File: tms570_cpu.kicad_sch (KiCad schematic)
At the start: 50 parts, among them J2 FTSH-105-01-L-DV-K, U2 TMS570LS0914PGE

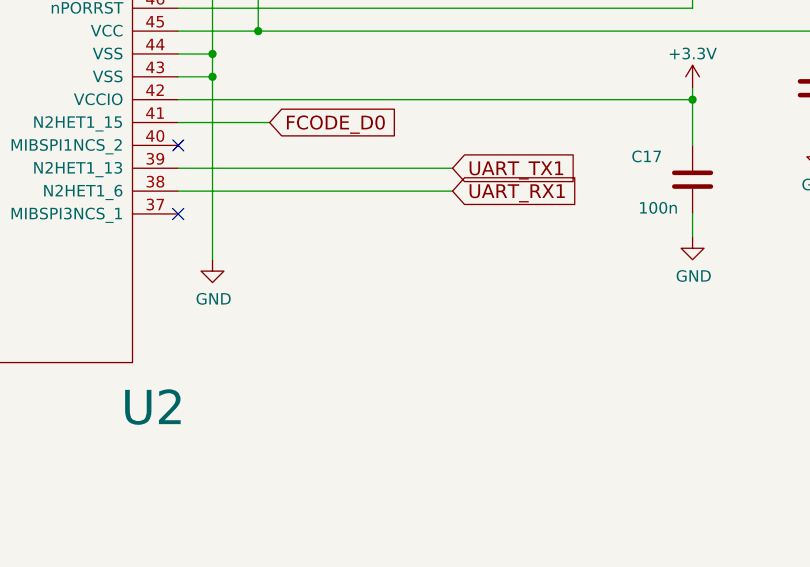
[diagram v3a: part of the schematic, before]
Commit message: Added a connector for the UART1 interface
Signed-off-by: Corey Minyard <corey@minyard.net>
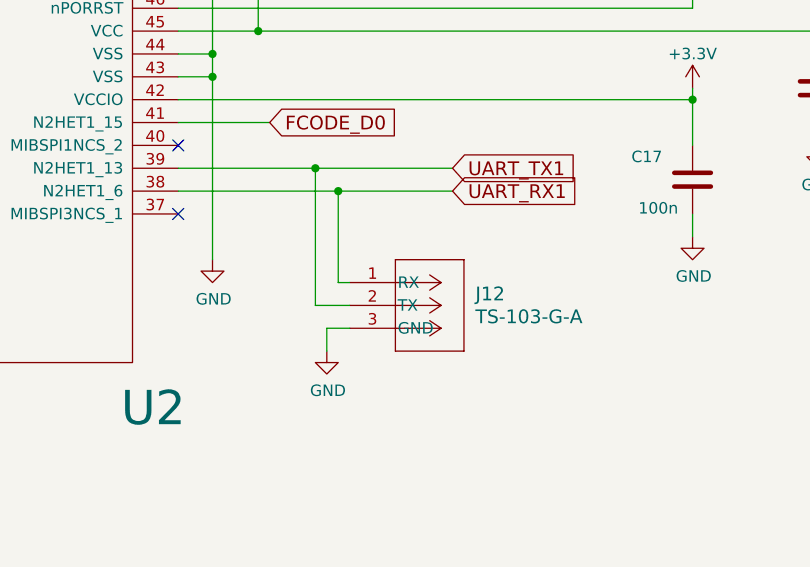
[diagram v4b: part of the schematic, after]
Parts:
- added J12: TS-103-G-A, LocalFootprints:CON3_1X3_TU_HTS_SAI, symbol PACSAT_DEV_misc:TS-103-G-A_2-UART
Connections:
- net GND: now also J12.3 (GND)
- net UART_RX1: now also J12.1 (RX)
- net UART_TX1: now also J12.2 (TX)
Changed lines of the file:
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@@
 	)
 	(junction
+		(at 297.18 177.8)
+		(diameter 0)
+		(color 0 0 0 0)
+	)
+	(junction
 		(at 237.49 207.01)
 		(diameter 0)
@@
 	)
 	(junction
+		(at 299.72 180.34)
+		(diameter 0)
+		(color 0 0 0 0)
+	)
+	(junction
 		(at 135.89 167.64)
 		(diameter 0)
@@
 	(wire
 		(pts
+			(xy 300.99 193.04) (xy 297.18 193.04)
+		)
+		(stroke
+			(width 0)
+			(type default)
+		)
+	)
+	(wire
+		(pts
 			(xy 140.97 76.2) (xy 101.6 76.2)
 		)
@@
 	(wire
 		(pts
-			(xy 281.94 180.34) (xy 312.42 180.34)
+			(xy 300.99 190.5) (xy 299.72 190.5)
+		)
+		(stroke
+			(width 0)
+			(type default)
+		)
+	)
+	(wire
+		(pts
+			(xy 281.94 180.34) (xy 299.72 180.34)
 		)
 		(stroke
@@
 	(wire
 		(pts
+			(xy 298.45 195.58) (xy 298.45 198.12)
+		)
+		(stroke
+			(width 0)
+			(type default)
+		)
+	)
+	(wire
+		(pts
 			(xy 101.6 142.24) (xy 149.86 142.24)
 		)
@@
 	(wire
 		(pts
-			(xy 281.94 177.8) (xy 312.42 177.8)
+			(xy 281.94 177.8) (xy 297.18 177.8)
 		)
 		(stroke
@@
 	(wire
 		(pts
+			(xy 299.72 180.34) (xy 312.42 180.34)
+		)
+		(stroke
+			(width 0)
+			(type default)
+		)
+	)
+	(wire
+		(pts
 			(xy 229.87 204.47) (xy 229.87 224.79)
 		)
@@
 		)
 	)
+	(wire
+		(pts
+			(xy 297.18 193.04) (xy 297.18 177.8)
+		)
+		(stroke
+			(width 0)
+			(type default)
+		)
+	)
 	(polyline
 		(pts
@@
 	(wire
 		(pts
+			(xy 297.18 177.8) (xy 312.42 177.8)
+		)
+		(stroke
+			(width 0)
+			(type default)
+		)
+	)
+	(wire
+		(pts
 			(xy 135.89 109.22) (xy 135.89 132.08)
 		)
@@
 	(wire
 		(pts
+			(xy 300.99 195.58) (xy 298.45 195.58)
+		)
+		(stroke
+			(width 0)
+			(type default)
+		)
+	)
+	(wire
+		(pts
 			(xy 121.92 139.7) (xy 149.86 139.7)
 		)
@@
 	(wire
 		(pts
+			(xy 299.72 190.5) (xy 299.72 180.34)
+		)
+		(stroke
+			(width 0)
+			(type default)
+		)
+	)
+	(wire
+		(pts
 			(xy 189.23 63.5) (xy 189.23 72.39)
 		)
@@
 	)
 	(symbol
+		(lib_id "PACSAT_DEV_misc:TS-103-G-A_2-UART")
+		(at 300.99 190.5 0)
+		(unit 1)
+		(exclude_from_sim no)
+		(in_bom yes)
+		(on_board yes)
+		(dnp no)
+		(fields_autoplaced yes)
+		(property "Reference" "J12"
+			(at 314.96 191.7699 0)
+			(effects
+				(font
+					(size 1.524 1.524)
+				)
+				(justify left)
+			)
+		)
+		(property "Value" "TS-103-G-A"
+			(at 314.96 194.3099 0)
+			(effects
+				(font
+					(size 1.524 1.524)
+				)
+				(justify left)
+			)
+		)
+		(property "Footprint" "LocalFootprints:CON3_1X3_TU_HTS_SAI"
+			(at 300.99 190.5 0)
+			(effects
+				(font
+					(size 1.27 1.27)
+					(italic yes)
+				)
+				(hide yes)
+			)
+		)
+		(property "Datasheet" "TS-103-G-A"
+			(at 300.99 190.5 0)
+			(effects
+				(font
+					(size 1.27 1.27)
+					(italic yes)
+				)
+				(hide yes)
+			)
+		)
+		(property "Description" "1x3 pin UART"
+			(at 300.99 190.5 0)
+			(effects
+				(font
+					(size 1.27 1.27)
+				)
+				(hide yes)
+			)
+		)
+		(pin "3"
+		)
+		(pin "2"
+		)
+		(pin "1"
+		)
+		(instances
+			(project ""
+				(path "/cc9f42d2-6985-41ac-acab-5ab7b01c5b38/adf61ae3-df77-4e04-8bda-b4049a36fcf4"
+					(reference "J12")
+					(unit 1)
+				)
+			)
+		)
+	)
+	(symbol
 		(lib_id "Device:R")
 		(at 228.6 24.13 0)
@@
 					(unit 1)
 				)
+			)
+		)
+	)
+	(symbol
+		(lib_id "power:GND")
+		(at 298.45 198.12 0)
+		(unit 1)
+		(exclude_from_sim no)
+		(in_bom yes)
+		(on_board yes)
+		(dnp no)
+		(property "Reference" "#PWR025"
+			(at 298.45 204.47 0)
+			(effects
+				(font
+					(size 1.27 1.27)
+				)
+				(hide yes)
+			)
+		)
+		(property "Value" "GND"
+			(at 298.577 202.5142 0)
+			(effects
+				(font
+					(size 1.27 1.27)
+				)
+			)
+		)
+		(property "Footprint" ""
+			(at 298.45 198.12 0)
+			(effects
+				(font
+					(size 1.27 1.27)
+				)
+				(hide yes)
+			)
+		)
+		(property "Datasheet" ""
+			(at 298.45 198.12 0)
+			(effects
+				(font
+					(size 1.27 1.27)
+				)
+				(hide yes)
+			)
+		)
+		(property "Description" ""
+			(at 298.45 198.12 0)
+			(effects
+				(font
+					(size 1.27 1.27)
+				)
+			)
+		)
+		(pin "1"
+		)
+		(instances
+			(project "PacSat_AFSK"
+				(path "/cc9f42d2-6985-41ac-acab-5ab7b01c5b38/adf61ae3-df77-4e04-8bda-b4049a36fcf4"
+					(reference "#PWR025")
+					(unit 1)
+				)

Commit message: Add 4 more MRAM parts
Signed-off-by: Corey Minyard <corey@minyard.net>
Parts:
- J12: footprint LocalFootprints:CON3_1X3_TU_HTS_SAI -> PacSatDev_misc:CON3_1X3_TU_HTS_SAI
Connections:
- net MRAM_NCS3: now reaches U2.37 (MIBSPI3NCS_1)
- net MRAM_NCS2: now reaches U2.40 (MIBSPI1NCS_2)
- net MRAM_NCS1: now reaches U2.54 (MIBSPI3NENA)
- net PWR_FLAG_LNA: now reaches U2.75 (AD1IN_11)
- no-connect marks 26 -> 22
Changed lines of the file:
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@@
 	)
 	(no_connect
-		(at 281.94 175.26)
-	)
-	(no_connect
 		(at 281.94 124.46)
 	)
@@
 	)
 	(no_connect
-		(at 281.94 182.88)
-	)
-	(no_connect
-		(at 281.94 139.7)
-	)
-	(no_connect
 		(at 227.33 72.39)
 	)
@@
 	)
 	(no_connect
-		(at 255.27 72.39)
-	)
-	(no_connect
 		(at 149.86 121.92)
 	)
@@
 	(wire
 		(pts
+			(xy 281.94 175.26) (xy 292.1 175.26)
+		)
+		(stroke
+			(width 0)
+			(type default)
+		)
+	)
+	(wire
+		(pts
 			(xy 281.94 134.62) (xy 285.75 134.62)
 		)
@@
 	(wire
 		(pts
+			(xy 281.94 182.88) (xy 303.53 182.88)
+		)
+		(stroke
+			(width 0)
+			(type default)
+		)
+	)
+	(wire
+		(pts
 			(xy 138.43 69.85) (xy 132.08 69.85)
 		)
@@
 	(wire
 		(pts
+			(xy 281.94 139.7) (xy 293.37 139.7)
+		)
+		(stroke
+			(width 0)
+			(type default)
+		)
+	)
+	(wire
+		(pts
 			(xy 229.87 68.58) (xy 229.87 72.39)
 		)
@@
 	(wire
 		(pts
+			(xy 255.27 68.58) (xy 255.27 72.39)
+		)
+		(stroke
+			(width 0)
+			(type default)
+		)
+	)
+	(wire
+		(pts
 			(xy 339.09 129.54) (xy 339.09 123.19)
 		)
@@
 		)
 	)
+	(global_label "MRAM_NCS1"
+		(shape input)
+		(at 293.37 139.7 0)
+		(fields_autoplaced yes)
+		(effects
+			(font
+				(size 1.524 1.524)
+			)
+			(justify left)
+		)
+		(property "Intersheetrefs" "${INTERSHEET_REFS}"
+			(at 309.665 139.7 0)
+			(effects
+				(font
+					(size 1.27 1.27)
+				)
+				(justify left)
+				(hide yes)
+			)
+		)
+	)
 	(global_label "AX5043_SEL2_N"
 		(shape input)
@@
 		)
 	)
+	(global_label "MRAM_NCS3"
+		(shape input)
+		(at 303.53 182.88 0)
+		(fields_autoplaced yes)
+		(effects
+			(font
+				(size 1.524 1.524)
+			)
+			(justify left)
+		)
+		(property "Intersheetrefs" "${INTERSHEET_REFS}"
+			(at 319.825 182.88 0)
+			(effects
+				(font
+					(size 1.27 1.27)
+				)
+				(justify left)
+				(hide yes)
+			)
+		)
+	)
 	(global_label "MRAM_MOSI"
 		(shape input)
@@
 		)
 	)
+	(global_label "MRAM_NCS2"
+		(shape input)
+		(at 292.1 175.26 0)
+		(fields_autoplaced yes)
+		(effects
+			(font
+				(size 1.524 1.524)
+			)
+			(justify left)
+		)
+		(property "Intersheetrefs" "${INTERSHEET_REFS}"
+			(at 308.395 175.26 0)
+			(effects
+				(font
+					(size 1.27 1.27)
+				)
+				(justify left)
+				(hide yes)
+			)
+		)
+	)
 	(global_label "MRAM_NCS0"
 		(shape input)
@@
 		)
 	)
+	(global_label "PWR_FLAG_LNA"
+		(shape input)
+		(at 255.27 68.58 90)
+		(fields_autoplaced yes)
+		(effects
+			(font
+				(size 1.524 1.524)
+			)
+			(justify left)
+		)
+		(property "Intersheetrefs" "${INTERSHEET_REFS}"
+			(at 255.27 49.1644 90)
+			(effects
+				(font
+					(size 1.27 1.27)
+				)
+				(justify left)
+				(hide yes)
+			)
+		)
+	)
 	(global_label "VER_BIT2"
 		(shape input)
@@
 			)
 		)
-		(property "Footprint" "LocalFootprints:CON3_1X3_TU_HTS_SAI"
+		(property "Footprint" "PacSatDev_misc:CON3_1X3_TU_HTS_SAI"
 			(at 300.99 190.5 0)
 			(effects

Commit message: Add a second CAN bus interface
Redundancy...

Signed-off-by: Corey Minyard <corey@minyard.net>
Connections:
- net CAN_B_TX: now reaches U2.128 (CAN2TX)
- net CAN_B_RX: now reaches U2.129 (CAN2RX)
- no-connect marks 22 -> 20
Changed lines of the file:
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@@
 	)
 	(no_connect
-		(at 149.86 144.78)
-	)
-	(no_connect
 		(at 247.65 68.58)
 	)
@@
 	)
 	(no_connect
-		(at 149.86 147.32)
-	)
-	(no_connect
 		(at 191.77 72.39)
 	)
@@
 	(wire
 		(pts
+			(xy 127 147.32) (xy 149.86 147.32)
+		)
+		(stroke
+			(width 0)
+			(type default)
+		)
+	)
+	(wire
+		(pts
 			(xy 191.77 204.47) (xy 191.77 226.06)
 		)
@@
 	(wire
 		(pts
+			(xy 127 144.78) (xy 149.86 144.78)
+		)
+		(stroke
+			(width 0)
+			(type default)
+		)
+	)
+	(wire
+		(pts
 			(xy 184.15 64.77) (xy 186.69 64.77)
 		)
@@
 		)
 	)
+	(global_label "CAN_B_TX"
+		(shape input)
+		(at 127 144.78 180)
+		(fields_autoplaced yes)
+		(effects
+			(font
+				(size 1.27 1.27)
+			)
+			(justify right)
+		)
+		(property "Intersheetrefs" "${INTERSHEET_REFS}"
+			(at 115.5976 144.78 0)
+			(effects
+				(font
+					(size 1.27 1.27)
+				)
+				(justify right)
+				(hide yes)
+			)
+		)
+	)
 	(global_label "VER_BIT1"
 		(shape input)
@@
 			(effects
 				(font
+					(size 1.27 1.27)
+				)
+				(justify right)
+				(hide yes)
+			)
+		)
+	)
+	(global_label "CAN_B_RX"
+		(shape input)
+		(at 127 147.32 180)
+		(fields_autoplaced yes)
+		(effects
+			(font
+				(size 1.27 1.27)
+			)
+			(justify right)
+		)
+		(property "Intersheetrefs" "${INTERSHEET_REFS}"
+			(at 115.2952 147.32 0)
+			(effects
+				(font

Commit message: Start working on active/standby handling
Signed-off-by: Corey Minyard <corey@minyard.net>
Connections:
- net OTHER_HW_POWER_OFF: now reaches U2.118 (N2HET1_10)
- net BOARD_NUM: now reaches U2.59 (AD1IN_17)
- net ACTIVE_N: now reaches U2.6 (N2HET1_11)
- net EXTERN_CONTROL: now reaches U2.62 (AD1IN_18)
- net GIOA_2 renamed OTHER_PRESENCE_N
- net GIOA_6 renamed OTHER_ACTIVE_N
- net GIOB_3 renamed OTHER_FAULT_N
- no-connect marks 20 -> 16
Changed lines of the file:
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@@
 	)
 	(no_connect
-		(at 281.94 127)
-	)
-	(no_connect
-		(at 184.15 204.47)
-	)
-	(no_connect
 		(at 247.65 68.58)
 	)
 	(no_connect
-		(at 149.86 119.38)
-	)
-	(no_connect
-		(at 281.94 119.38)
-	)
-	(no_connect
 		(at 281.94 99.06)
 	)
@@
 	(wire
 		(pts
-			(xy 191.77 204.47) (xy 191.77 226.06)
+			(xy 191.77 204.47) (xy 191.77 233.68)
 		)
 		(stroke
@@
 	(wire
 		(pts
+			(xy 125.73 119.38) (xy 149.86 119.38)
+		)
+		(stroke
+			(width 0)
+			(type default)
+		)
+	)
+	(wire
+		(pts
 			(xy 110.49 198.12) (xy 110.49 201.93)
 		)
@@
 	(wire
 		(pts
-			(xy 209.55 204.47) (xy 209.55 223.52)
+			(xy 209.55 204.47) (xy 209.55 233.68)
 		)
 		(stroke
@@
 	(wire
 		(pts
+			(xy 184.15 204.47) (xy 184.15 233.68)
+		)
+		(stroke
+			(width 0)
+			(type default)
+		)
+	)
+	(wire
+		(pts
 			(xy 99.06 111.76) (xy 99.06 116.84)
 		)
@@
 	(wire
 		(pts
+			(xy 281.94 127) (xy 288.29 127)
+		)
+		(stroke
+			(width 0)
+			(type default)
+		)
+	)
+	(wire
+		(pts
 			(xy 121.92 139.7) (xy 149.86 139.7)
 		)
@@
 	(wire
 		(pts
-			(xy 171.45 247.65) (xy 171.45 204.47)
+			(xy 171.45 233.68) (xy 171.45 204.47)
 		)
 		(stroke
@@
 	(wire
 		(pts
+			(xy 281.94 119.38) (xy 288.29 119.38)
+		)
+		(stroke
+			(width 0)
+			(type default)
+		)
+	)
+	(wire
+		(pts
 			(xy 285.75 165.1) (xy 285.75 167.64)
 		)
@@
 		)
 	)
+	(global_label "OTHER_HW_POWER_OFF"
+		(shape input)
+		(at 125.73 119.38 180)
+		(fields_autoplaced yes)
+		(effects
+			(font
+				(size 1.524 1.524)
+			)
+			(justify right)
+		)
+		(property "Intersheetrefs" "${INTERSHEET_REFS}"
+			(at 96.88 119.38 0)
+			(effects
+				(font
+					(size 1.27 1.27)
+				)
+				(justify right)
+				(hide yes)
+			)
+		)
+	)
 	(global_label "MRAM_NCS1"
 		(shape input)
@@
 		)
 	)
-	(global_label "GIOA_6"
-		(shape input)
-		(at 209.55 223.52 270)
-		(fields_autoplaced yes)
-		(effects
-			(font
-				(size 1.524 1.524)
-			)
-			(justify right)
-		)
-		(property "Intersheetrefs" "${INTERSHEET_REFS}"
-			(at 209.55 233.9865 90)
-			(effects
-				(font
-					(size 1.27 1.27)
-				)
-				(justify right)
-				(hide yes)
-			)
-		)
-	)
 	(global_label "MRAM_CLK"
 		(shape input)
@@
 		)
 	)
+	(global_label "OTHER_ACTIVE_N"
+		(shape input)
+		(at 209.55 233.68 270)
+		(fields_autoplaced yes)
+		(effects
+			(font
+				(size 1.524 1.524)
+			)
+			(justify right)
+		)
+		(property "Intersheetrefs" "${INTERSHEET_REFS}"
+			(at 209.55 255.0551 90)
+			(effects
+				(font
+					(size 1.27 1.27)
+				)
+				(justify right)
+				(hide yes)
+			)
+		)
+	)
 	(global_label "UART_TX1"
 		(shape input)
@@
 		)
 	)
+	(global_label "OTHER_PRESENCE_N"
+		(shape input)
+		(at 191.77 233.68 270)
+		(fields_autoplaced yes)
+		(effects
+			(font
+				(size 1.524 1.524)
+			)
+			(justify right)
+		)
+		(property "Intersheetrefs" "${INTERSHEET_REFS}"
+			(at 191.77 259.4095 90)
+			(effects
+				(font
+					(size 1.27 1.27)
+				)
+				(justify right)
+				(hide yes)
+			)
+		)
+	)
 	(global_label "AX5043_EN_RX3_N"
 		(shape input)
@@
 		)
 	)
+	(global_label "ACTIVE_N"
+		(shape input)
+		(at 184.15 233.68 270)
+		(fields_autoplaced yes)
+		(effects
+			(font
+				(size 1.524 1.524)
+			)
+			(justify right)
+		)
+		(property "Intersheetrefs" "${INTERSHEET_REFS}"
+			(at 184.15 246.6368 90)
+			(effects
+				(font
+					(size 1.27 1.27)
+				)
+				(justify right)
+				(hide yes)
+			)
+		)
+	)
 	(global_label "MRAM_MISO"
 		(shape input)
@@
 		)
 	)
-	(global_label "GIOA_2"
-		(shape input)
-		(at 191.77 226.06 270)
-		(fields_autoplaced yes)
-		(effects
-			(font
-				(size 1.524 1.524)
-			)
-			(justify right)
-		)
-		(property "Intersheetrefs" "${INTERSHEET_REFS}"
-			(at 191.77 236.5265 90)
-			(effects
-				(font
-					(size 1.27 1.27)
-				)
-				(justify right)
-				(hide yes)
-			)
-		)
-	)
-	(global_label "GIOB_3"
+	(global_label "OTHER_FAULT_N"
 		(shape input)
-		(at 171.45 247.65 270)
+		(at 171.45 233.68 270)
 		(fields_autoplaced yes)
 		(effects
@@
 		)
 		(property "Intersheetrefs" "${INTERSHEET_REFS}"
-			(at 171.45 258.3342 90)
+			(at 171.45 254.2568 90)
 			(effects
 				(font
@@
 		)
 	)
+	(global_label "BOARD_NUM"
+		(shape input)
+		(at 288.29 127 0)
+		(fields_autoplaced yes)
+		(effects
+			(font
+				(size 1.524 1.524)
+			)
+			(justify left)
+		)
+		(property "Intersheetrefs" "${INTERSHEET_REFS}"
+			(at 304.6577 127 0)
+			(effects
+				(font
+					(size 1.27 1.27)
+				)
+				(justify left)
+				(hide yes)
+			)
+		)
+	)
 	(global_label "VER_BIT3"
 		(shape input)
@@
 				(hide yes)
 			)
+		)
+	)
+	(global_label "EXTERN_CONTROL"
+		(shape input)
+		(at 288.29 119.38 0)
+		(fields_autoplaced yes)
+		(effects
+			(font
+				(size 1.524 1.524)
+			)
+			(justify left)
+		)
+		(property "Intersheetrefs" "${INTERSHEET_REFS}"
+			(at 310.9714 119.38 0)
+			(effects
+				(font
+					(size 1.27 1.27)
+				)
+				(justify left)
+				(hide yes)
+			)
